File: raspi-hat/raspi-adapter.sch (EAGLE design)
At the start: 37 parts, among them IC1 24C01SN, Q1 BSS138

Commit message: review schematic and layout
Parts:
- removed JP12, JP15, JP9: (no value), SparkFun-Passives:JUMPER-2PTH
- removed L1, L2, L3, L4: WS2812B, adafruit:WS2812B
- added X10, X2: (no value), adafruit:PINHD-1X3
- added X4: (no value), adafruit:PINHD-1X8CLEANBIG
- added X8: (no value), adafruit:PINHD-1X6B
- added X9: HAT-Conn, adafruit:PINHD-2X20
- C1: value 1u -> 100u; device rcl:C-EUC0603 -> rcl:C-EUC1210
- C2: value 10n -> 1u
- C3: value 100u -> 10n; device rcl:C-EUC1210 -> rcl:C-EUC0603
- JP1: value HAT-Conn -> (none); device adafruit:PINHD-2X20 -> SparkFun-Passives:JUMPER-2PTH
- JP2: device adafruit:PINHD-1X8CLEANBIG -> SparkFun-Passives:JUMPER-2PTH
- JP3: device adafruit:PINHD-1X6B -> SparkFun-Passives:JUMPER-2PTH
- JP5: device adafruit:PINHD-1X3 -> SparkFun-Passives:JUMPER-2PTH
- R2: value 3k9 -> 270
- R5: value 270 -> 3k9
- renumbered JP10 to X6, JP11 to X7, JP13 to X11, JP14 to X1, JP8 to X3, SW3 to SW1, SW4 to SW2, U$3 to X5
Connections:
- removed net N$1: L2.DOUT, L3.DIN
- removed net N$3: L3.DOUT, L4.DIN
- removed net N$5: L1.DIN, Q1.D, R5.1
- removed net N$9: JP4.1, VEXT+.1
- new net +5V: C1.1, R2.2, V+NEO.1, X2.2
- new net 3V3_RPI: JP2.2, X9.1, X9.17
- new net VIN_RPI: JP1.2, X9.2, X9.4
- net +3V3: now also C3.1, JP2.1, R5.2; no longer C2.1, JP1.1, JP1.17, R2.2
- net GND: now also X8.1, X9.14, X9.20, X9.25, X9.30, X9.34, X9.39, X9.6, X9.9; no longer JP1.14, JP1.20, JP1.25, JP1.30, JP1.34, JP1.39, JP1.6, JP1.9, JP3.1, L1.GND, L2.GND, L3.GND, L4.GND
- net LED_BLUE: now also X10.1, X9.35; no longer JP1.35, JP5.1
- net LED_GREEN: now also X10.3, X9.40; no longer JP1.40, JP5.3
- net LED_RED: now also X9.15; no longer JP1.15
- net LED_YELLOW: now also X10.2, X9.38; no longer JP1.38, JP5.2
- net N$2: now also VEXT+.1, X2.1; no longer L1.DOUT, L2.DIN
- net N$6: now also Q1.D, R2.1; no longer L4.DOUT
- net N$7: now also JP4.1, X9.16; no longer JP1.16, JP7.1
- net RST: now also JP4.2; no longer JP7.2
- net SCL: now also JP3.2, R4.1; no longer JP6.2, R3.1
- net SDA: now also JP7.1, R5.1; no longer JP15.1, R2.1
- net V+: now also C2.1, JP1.1, X2.3; no longer C1.1, C3.1, JP1.2, JP1.4, JP4.2, L1.VDD, L2.VDD, L3.VDD, L4.VDD, R5.2, V+NEO.1
- net X1: now also JP5.1, X4.8, X9.5; no longer JP1.5, JP12.1, JP2.8
- net X1_: now also JP5.2, X9.8; no longer JP1.8, JP12.2
- net X2: now also JP6.1, X4.7, X9.3; no longer JP1.3, JP2.7, JP9.1
- net X2_2: now also JP6.2, X9.10; no longer JP1.10, JP9.2
- net X3: now also X4.6, X9.11; no longer JP1.11, JP2.6
- net X4: now also X4.5, X9.13; no longer JP1.13, JP2.5
- net X5: now also R3.1, X4.4; no longer JP2.4, R4.1
- net X6: now also X4.3; no longer JP2.3
- net X7: now also X4.2; no longer JP2.2
- net X8: now also X4.1; no longer JP2.1
- net Y1: now also X8.5; no longer JP3.5
- net Y10: now also JP7.2, X9.27; no longer JP1.27, JP15.2
- net Y2: now also X8.4; no longer JP3.4
- net Y3: now also X9.12; no longer JP1.12
- net Y4: now also X9.7; no longer JP1.7
- net Y5: now also X9.24; no longer JP1.24
- net Y6: now also X9.23; no longer JP1.23
- net Y7: now also X9.21; no longer JP1.21
- net Y8: now also X9.19; no longer JP1.19
- net Y9: now also JP3.1, X9.28; no longer JP1.28, JP6.1
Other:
- moved on the sheet: C1, C2, C3, DIN_NEO, JP4, JP6, JP7, Q1, R1, R2, R3, R4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

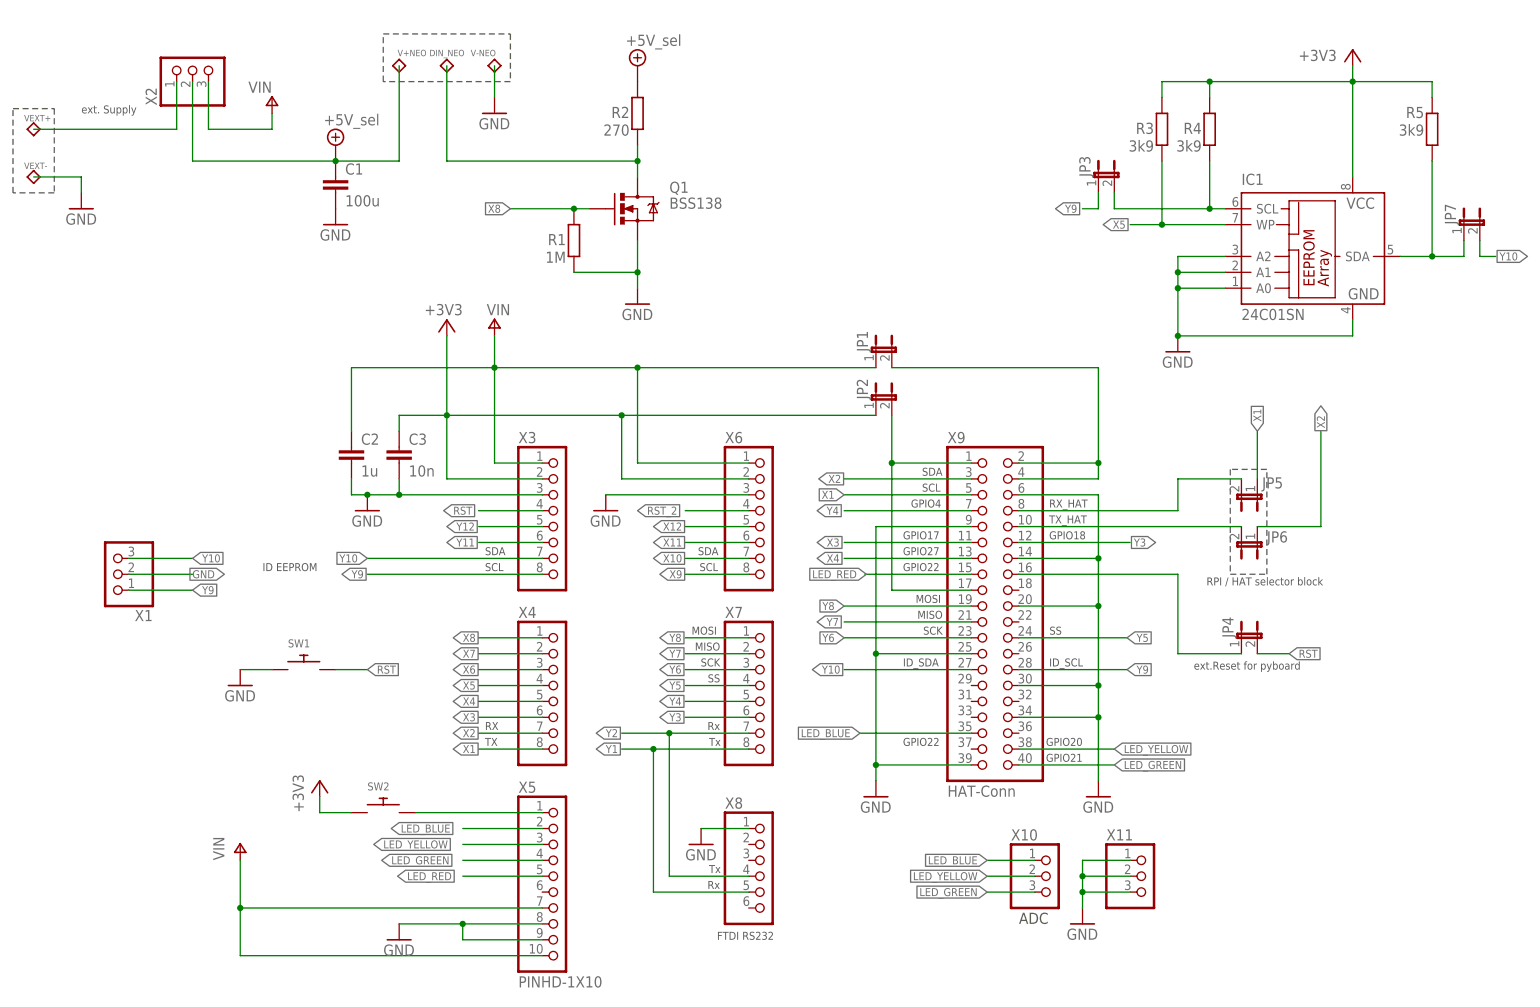
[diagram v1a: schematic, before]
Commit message: working in review, removed onboard neopixel
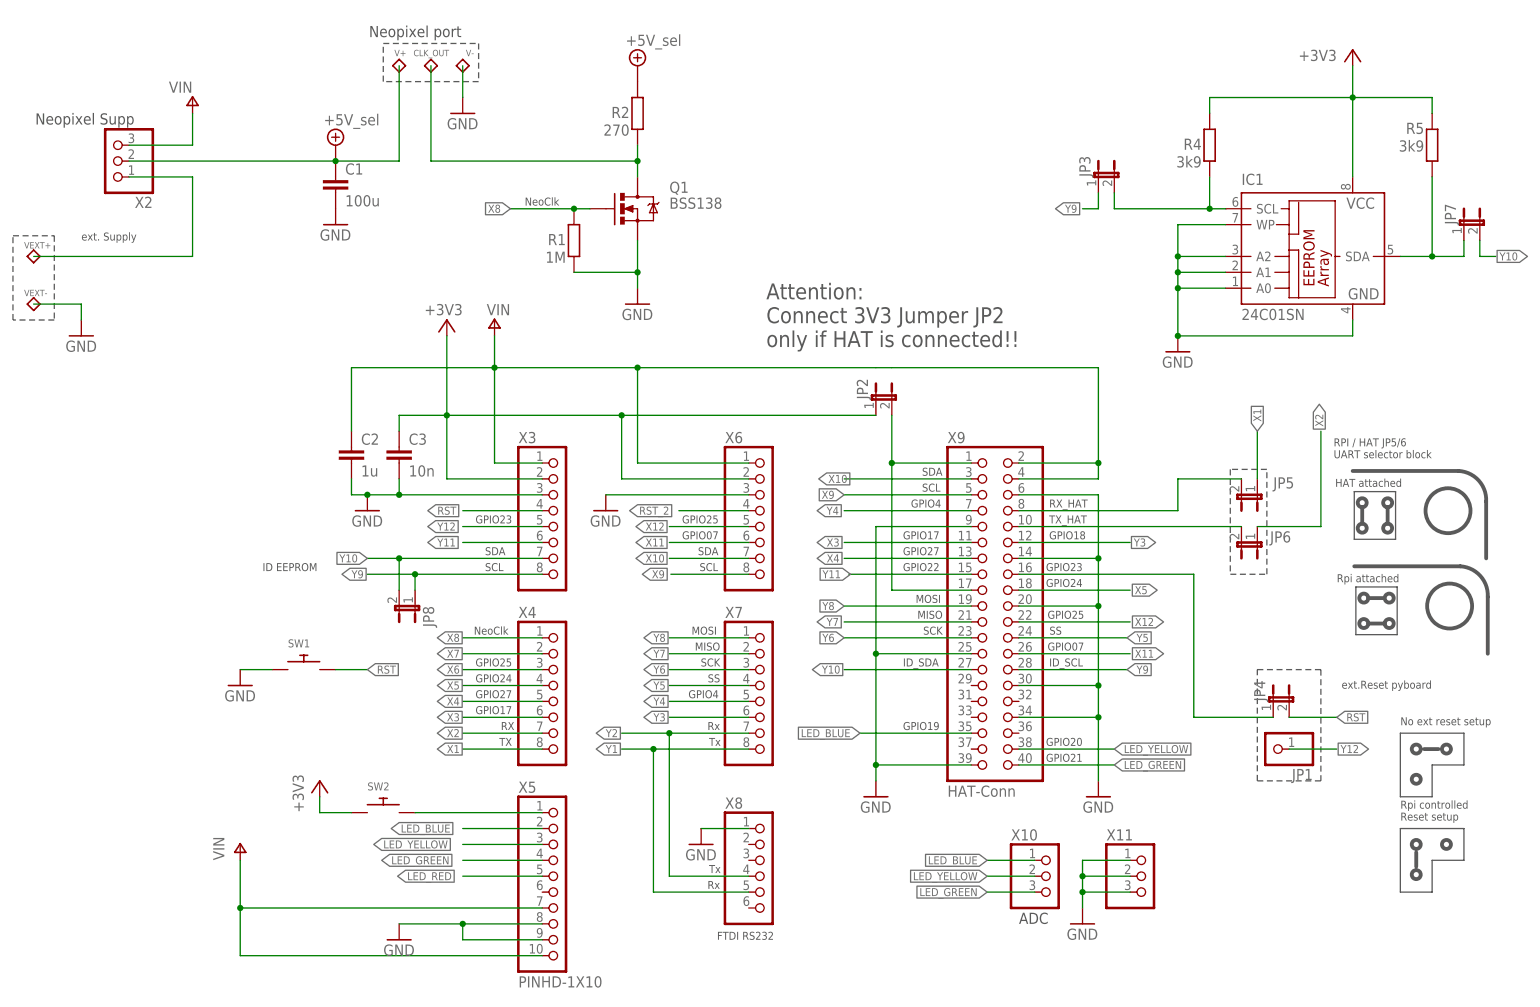
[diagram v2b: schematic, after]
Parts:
- removed DIN_NEO, V-NEO: TP_BATT, GasDemo:TP_BATT
- removed R3: 3k9, resistor:R-EU_R0603
- removed X1: (no value), adafruit:PINHD-1X3
- added CLK_OUT, V-: TP_BATT, GasDemo:TP_BATT
- added JP8: (no value), SparkFun-Passives:JUMPER-2PTH
- C1: device rcl:C-EUC1210 -> rcl:C-EUC2220K
- JP1: device SparkFun-Passives:JUMPER-2PTH -> adafruit:PINHD-1X1
- V+: value V+NEO -> V+
- renumbered V+NEO to V+
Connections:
- removed net VIN_RPI: JP1.2, X9.2, X9.4
- net +3V3: no longer R3.2
- net GND: now also IC1.WP, V-.1; no longer V-NEO.1, X1.2
- net LED_RED: no longer X9.15
- net N$6: now also CLK_OUT.1; no longer DIN_NEO.1
- net V+: now also X9.2, X9.4; no longer JP1.1
- net X1: no longer X9.5
- net X10: now also X9.3
- net X11: now also X9.26
- net X12: now also X9.22
- net X2: no longer X9.3
- net X5: now also X9.18; no longer IC1.WP, R3.1
- net X9: now also X9.5
- net Y10: now also JP8.2; no longer X1.3
- net Y11: now also X9.15
- net Y12: now also JP1.1
- net Y9: now also JP8.1; no longer X1.1
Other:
- note added: "Attention: Connect 3V3 Jumper JP2 only if HAT is connected!!"
- note added: "GPIO07"
- note added: "GPIO19"
- note added: "GPIO23"
- note added: "GPIO24"
- note added: "GPIO25"
- note added: "HAT attached"
- note added: "NeoClk"
- note added: "Neopixel Supp"
- note added: "Neopixel port"
- note added: "No ext reset setup"
- note added: "RPI / HAT JP5/6 UART selector block"
- note added: "Rpi attached"
- note added: "Rpi controlled Reset setup"
- note added: "ext.Reset pyboard"
- note removed: "RPI / HAT selector block"
- note removed: "ext.Reset for pyboard"
- moved on the sheet: JP4, R4, R5, VEXT+, VEXT-, X2
